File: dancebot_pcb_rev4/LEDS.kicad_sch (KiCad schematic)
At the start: 4 parts, among them J4 NeoPixel Left Eye, J9 NeoPixel Left Eye

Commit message: schematic ready for review!
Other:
- note added: "Hierarchical Labels"
- moved on the sheet: LED1, R11

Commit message: implemented some changes
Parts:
- added LED2: APT2012PGW, SamacSys_Parts:APT2012PGW, symbol Device:LED
- added R8: 1k, SamacSys_Parts:RESC2012X60N, symbol Device:R
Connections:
- net GND: now also R8.2
- new net: LED2.1 (K), R8.1
- new net IO45: LED2.2 (A)
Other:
- note added: "Heartbeat LED"

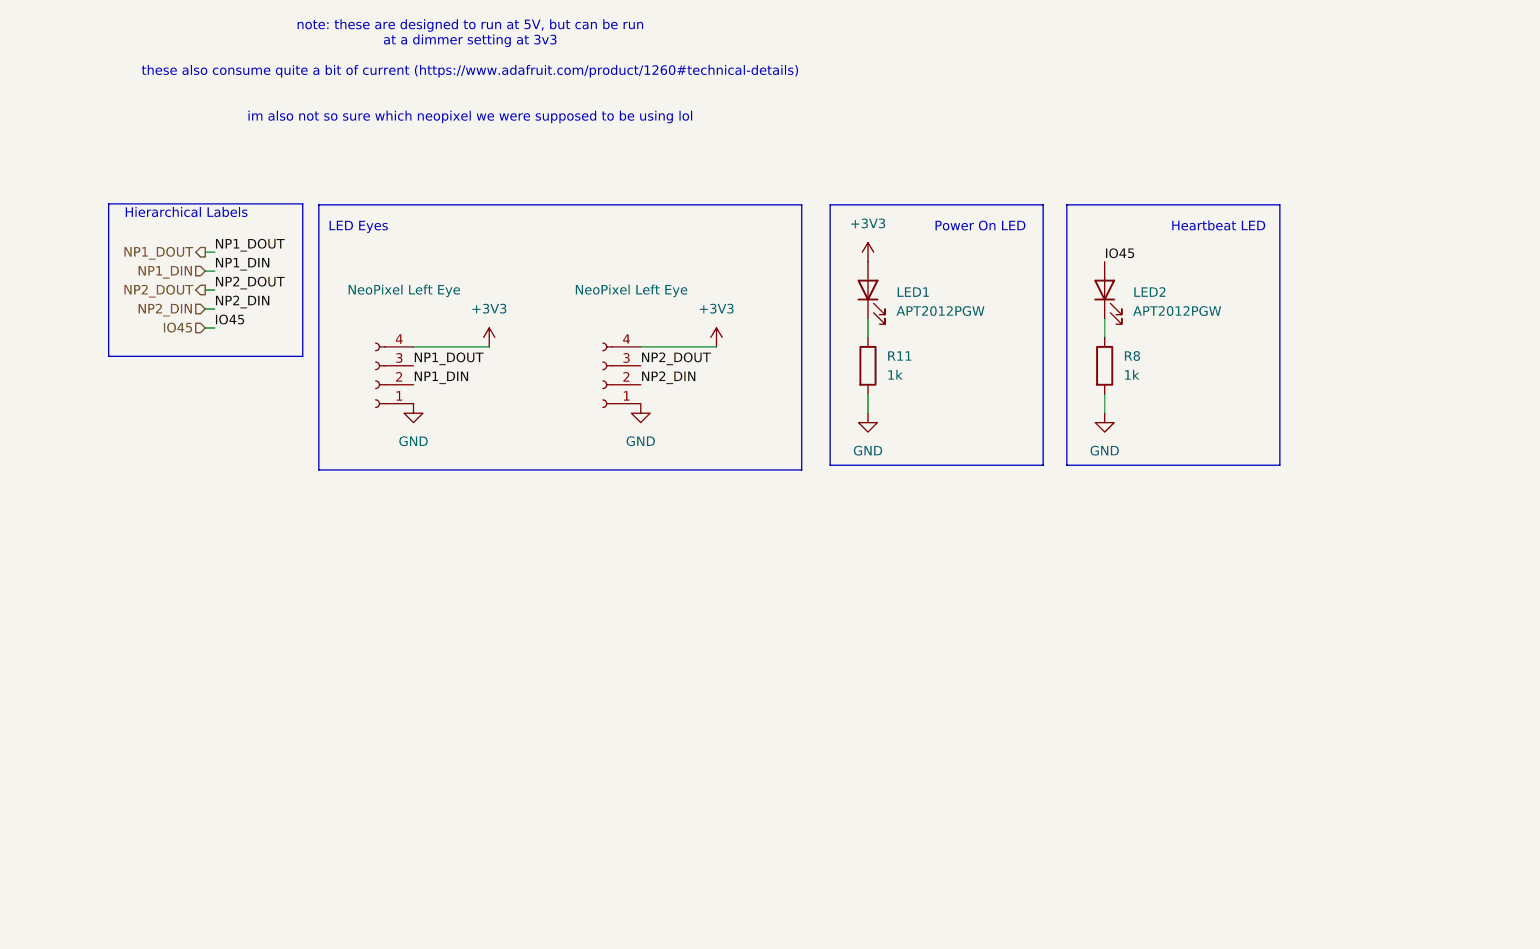
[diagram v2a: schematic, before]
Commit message: added more power leds. need to finish routing. fixed 3d models
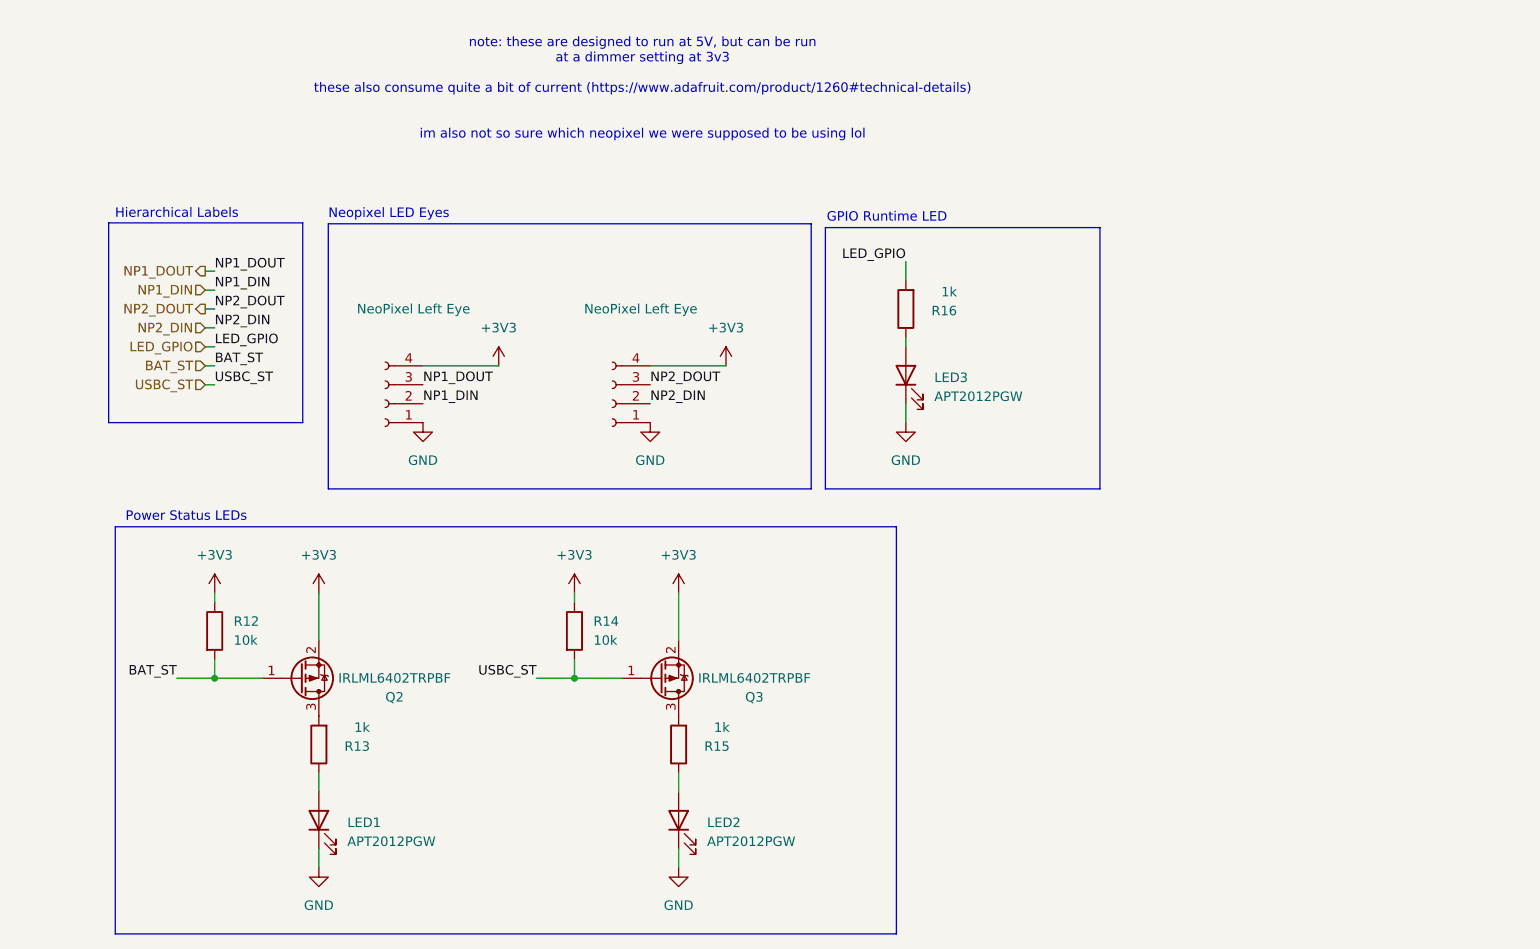
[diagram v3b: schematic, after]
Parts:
- removed R11, R8: 1k, SamacSys_Parts:RESC2012X60N, symbol Device:R
- added LED3: APT2012PGW, SamacSys_Parts:APT2012PGW, symbol Device:LED
- added Q2, Q3: IRLML6402TRPBF, Package_TO_SOT_SMD:SOT-23, symbol Transistor_FET:IRLML6402
- added R12, R14: 10k, SamacSys_Parts:RESC2012X60N, symbol Device:R
- added R13, R15, R16: 1k, SamacSys_Parts:RESC2012X60N, symbol Device:R
- renumbered J4 to J10
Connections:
- net +3V3: now also Q2.2 (S), Q3.2 (S), R12.1, R14.1; no longer LED1.2 (A)
- net GND: now also LED1.1 (K), LED2.1 (K), LED3.1 (K)
- net IO45: no longer names the net of LED2.2 (A)
- net IO45: now also R15.1
- new net: Q3.3 (D), R15.2
- new net: Q2.3 (D), R13.2
- new net: LED1.2 (A), R13.1
- new net: LED3.2 (A), R16.1
- new net BAT_ST: Q2.1 (G), R12.2
- new net LED_GPIO: R16.2
- new net USBC_ST: Q3.1 (G), R14.2
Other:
- note added: "GPIO Runtime LED"
- note added: "Neopixel LED Eyes"
- note added: "Power Status LEDs"
- note removed: "Heartbeat LED"
- note removed: "LED Eyes"
- note removed: "Power On LED"

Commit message: finished first layout. need to add polygon pours
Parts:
- J10: value NeoPixel Left Eye -> NeoPixel Right Eye
- renumbered Q2 to Q3, Q3 to Q4
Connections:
- net +3V3: now also J10.2 (Pin_2), J9.2 (Pin_2); no longer J10.4 (Pin_4), J9.4 (Pin_4)
- net NP1_DIN: now also J9.4 (Pin_4); no longer J9.2 (Pin_2)
- net NP2_DIN: now also J10.4 (Pin_4); no longer J10.2 (Pin_2)
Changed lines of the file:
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@@
 	(wire
 		(pts
-			(xy 86.36 36.83) (xy 96.52 36.83)
+			(xy 120.65 33.02) (xy 120.65 34.29)
 		)
 		(stroke
@@
 	(wire
 		(pts
-			(xy 120.65 33.02) (xy 120.65 34.29)
+			(xy 90.17 93.98) (xy 90.17 91.44)
 		)
 		(stroke
@@
 	(wire
 		(pts
-			(xy 90.17 93.98) (xy 90.17 91.44)
+			(xy 90.17 67.31) (xy 90.17 73.66)
 		)
 		(stroke
@@
 	(wire
 		(pts
-			(xy 90.17 67.31) (xy 90.17 73.66)
+			(xy 41.91 91.44) (xy 41.91 93.98)
 		)
 		(stroke
@@
 	(wire
 		(pts
-			(xy 41.91 91.44) (xy 41.91 93.98)
+			(xy 27.94 67.31) (xy 27.94 68.58)
 		)
 		(stroke
@@
 	(wire
 		(pts
-			(xy 27.94 67.31) (xy 27.94 68.58)
+			(xy 76.2 67.31) (xy 76.2 68.58)
 		)
 		(stroke
@@
 	(wire
 		(pts
-			(xy 76.2 67.31) (xy 76.2 68.58)
+			(xy 76.2 76.2) (xy 76.2 78.74)
 		)
 		(stroke
@@
 	(wire
 		(pts
-			(xy 76.2 76.2) (xy 76.2 78.74)
+			(xy 86.36 41.91) (xy 96.52 41.91)
 		)
 		(stroke
@@
 	(wire
 		(pts
-			(xy 55.88 36.83) (xy 66.04 36.83)
+			(xy 26.67 36.83) (xy 27.94 36.83)
 		)
 		(stroke
@@
 	(wire
 		(pts
-			(xy 26.67 36.83) (xy 27.94 36.83)
+			(xy 26.67 39.37) (xy 27.94 39.37)
 		)
 		(stroke
@@
 	(wire
 		(pts
-			(xy 26.67 39.37) (xy 27.94 39.37)
+			(xy 27.94 78.74) (xy 34.29 78.74)
 		)
 		(stroke
@@
 	(wire
 		(pts
-			(xy 27.94 78.74) (xy 34.29 78.74)
+			(xy 27.94 26.67) (xy 26.67 26.67)
 		)
 		(stroke
@@
 	(wire
 		(pts
-			(xy 27.94 26.67) (xy 26.67 26.67)
+			(xy 41.91 67.31) (xy 41.91 73.66)
 		)
 		(stroke
@@
 	(wire
 		(pts
-			(xy 41.91 67.31) (xy 41.91 73.66)
+			(xy 76.2 78.74) (xy 82.55 78.74)
 		)
 		(stroke
@@
 	(wire
 		(pts
-			(xy 76.2 78.74) (xy 82.55 78.74)
+			(xy 67.31 41.91) (xy 55.88 41.91)
 		)
 		(stroke
@@
 	)
 	(label "NP2_DIN"
-		(at 86.36 41.91 0)
+		(at 86.36 36.83 0)
 		(effects
 			(font
@@
 	)
 	(label "NP1_DIN"
-		(at 55.88 41.91 0)
+		(at 55.88 36.83 0)
 		(effects
 			(font
@@
 			)
 		)
-		(property "Value" "NeoPixel Left Eye"
-			(at 85.09 29.21 0)
+		(property "Value" "NeoPixel Right Eye"
+			(at 87.884 32.258 0)
 			(effects
 				(font
@@
 		(on_board yes)
 		(dnp no)
-		(property "Reference" "Q3"
+		(property "Reference" "Q4"
 			(at 100.33 81.28 0)
 			(effects
@@
 			(project "Dancebot_PCB"
 				(path "/21324b60-e5e7-4de6-a38d-f4cdf81a1b2c/d46550a5-946a-497c-941e-91cb76bf7d90"
-					(reference "Q3")
+					(reference "Q4")
 					(unit 1)
 				)
@@
 		)
 		(property "Value" "NeoPixel Left Eye"
-			(at 54.61 29.21 0)
+			(at 57.15 32.766 0)
 			(effects
 				(font
@@
 		(dnp no)
 		(fields_autoplaced yes)
-		(property "Reference" "#PWR050"
+		(property "Reference" "#PWR054"
 			(at 55.88 50.8 0)
 			(effects
@@
 			(project ""
 				(path "/21324b60-e5e7-4de6-a38d-f4cdf81a1b2c/d46550a5-946a-497c-941e-91cb76bf7d90"
-					(reference "#PWR050")
+					(reference "#PWR054")
 					(unit 1)
 				)
@@
 		(dnp no)
 		(fields_autoplaced yes)
-		(property "Reference" "#PWR057"
+		(property "Reference" "#PWR061"
 			(at 120.65 50.8 0)
 			(effects
@@
 			(project "Dancebot_PCB"
 				(path "/21324b60-e5e7-4de6-a38d-f4cdf81a1b2c/d46550a5-946a-497c-941e-91cb76bf7d90"
-					(reference "#PWR057")
+					(reference "#PWR061")
 					(unit 1)
 				)
@@
 	(symbol
 		(lib_id "power:+3V3")
-		(at 66.04 36.83 0)
+		(at 67.31 41.91 0)
 		(unit 1)
 		(exclude_from_sim no)
@@
 		(on_board yes)
 		(dnp no)
-		(fields_autoplaced yes)
-		(property "Reference" "#PWR051"
-			(at 66.04 40.64 0)
+		(property "Reference" "#PWR055"
+			(at 67.31 45.72 0)
 			(effects
 				(font
@@
 		)
 		(property "Value" "+3V3"
-			(at 66.04 31.75 0)
+			(at 69.342 38.1 0)
 			(effects
 				(font
@@
 		)
 		(property "Footprint" ""
-			(at 66.04 36.83 0)
+			(at 67.31 41.91 0)
 			(effects
 				(font
@@
 		)
 		(property "Datasheet" ""
-			(at 66.04 36.83 0)
+			(at 67.31 41.91 0)
 			(effects
 				(font
@@
 		)
 		(property "Description" "Power symbol creates a global label with name \"+3V3\""
-			(at 66.04 36.83 0)
+			(at 67.31 41.91 0)
 			(effects
 				(font
@@
 			(project ""
 				(path "/21324b60-e5e7-4de6-a38d-f4cdf81a1b2c/d46550a5-946a-497c-941e-91cb76bf7d90"
-					(reference "#PWR051")
+					(reference "#PWR055")
 					(unit 1)
 				)
@@
 		(on_board yes)
 		(dnp no)
-		(property "Reference" "Q2"
+		(property "Reference" "Q3"
 			(at 52.07 81.28 0)
 			(effects
@@
 			(project "Dancebot_PCB"
 				(path "/21324b60-e5e7-4de6-a38d-f4cdf81a1b2c/d46550a5-946a-497c-941e-91cb76bf7d90"
-					(reference "Q2")
+					(reference "Q3")
 					(unit 1)
 				)
@@
 	(symbol
 		(lib_id "power:+3V3")
-		(at 96.52 36.83 0)
+		(at 96.52 41.91 0)
 		(unit 1)
 		(exclude_from_sim no)
@@
 		(on_board yes)
 		(dnp no)
-		(fields_autoplaced yes)
-		(property "Reference" "#PWR056"
-			(at 96.52 40.64 0)
+		(property "Reference" "#PWR060"
+			(at 96.52 45.72 0)
 			(effects
 				(font
@@
 		)
 		(property "Value" "+3V3"
-			(at 96.52 31.75 0)
+			(at 100.33 39.37 0)
 			(effects
 				(font
@@
 		)
 		(property "Footprint" ""
-			(at 96.52 36.83 0)
+			(at 96.52 41.91 0)
 			(effects
 				(font
@@
 		)
 		(property "Datasheet" ""
-			(at 96.52 36.83 0)
+			(at 96.52 41.91 0)
 			(effects
 				(font
@@
 		)
 		(property "Description" "Power symbol creates a global label with name \"+3V3\""
-			(at 96.52 36.83 0)
+			(at 96.52 41.91 0)
 			(effects
 				(font
@@
 			(project "Dancebot_PCB"
 				(path "/21324b60-e5e7-4de6-a38d-f4cdf81a1b2c/d46550a5-946a-497c-941e-91cb76bf7d90"
-					(reference "#PWR056")
+					(reference "#PWR060")
 					(unit 1)
 				)
@@
 		(dnp no)
 		(fields_autoplaced yes)
-		(property "Reference" "#PWR049"
+		(property "Reference" "#PWR053"
 			(at 41.91 110.49 0)
 			(effects
@@
 			(project "Dancebot_PCB"
 				(path "/21324b60-e5e7-4de6-a38d-f4cdf81a1b2c/d46550a5-946a-497c-941e-91cb76bf7d90"
-					(reference "#PWR049")
+					(reference "#PWR053")
 					(unit 1)
 				)
@@
 		(dnp no)
 		(fields_autoplaced yes)
-		(property "Reference" "#PWR047"
+		(property "Reference" "#PWR051"
 			(at 27.94 71.12 0)
 			(effects
@@
 			(project "Dancebot_PCB"
 				(path "/21324b60-e5e7-4de6-a38d-f4cdf81a1b2c/d46550a5-946a-497c-941e-91cb76bf7d90"
-					(reference "#PWR047")
+					(reference "#PWR051")
 					(unit 1)
 				)
@@
 		(dnp no)
 		(fields_autoplaced yes)
-		(property "Reference" "#PWR055"
+		(property "Reference" "#PWR059"
 			(at 90.17 110.49 0)
 			(effects
@@
 			(project "Dancebot_PCB"
 				(path "/21324b60-e5e7-4de6-a38d-f4cdf81a1b2c/d46550a5-946a-497c-941e-91cb76bf7d90"
-					(reference "#PWR055")
+					(reference "#PWR059")
 					(unit 1)
 				)
@@
 		(dnp no)
 		(fields_autoplaced yes)
-		(property "Reference" "#PWR048"
+		(property "Reference" "#PWR052"
 			(at 41.91 71.12 0)
 			(effects
@@
 			(project "Dancebot_PCB"
 				(path "/21324b60-e5e7-4de6-a38d-f4cdf81a1b2c/d46550a5-946a-497c-941e-91cb76bf7d90"
-					(reference "#PWR048")
+					(reference "#PWR052")
 					(unit 1)
 				)
@@
 		(dnp no)
 		(fields_autoplaced yes)
-		(property "Reference" "#PWR054"
+		(property "Reference" "#PWR058"
 			(at 90.17 71.12 0)
 			(effects
@@
 			(project "Dancebot_PCB"
 				(path "/21324b60-e5e7-4de6-a38d-f4cdf81a1b2c/d46550a5-946a-497c-941e-91cb76bf7d90"
-					(reference "#PWR054")
+					(reference "#PWR058")
 					(unit 1)
 				)
@@
 		(dnp no)
 		(fields_autoplaced yes)
-		(property "Reference" "#PWR052"
+		(property "Reference" "#PWR056"
 			(at 76.2 71.12 0)
 			(effects
@@
 			(project "Dancebot_PCB"
 				(path "/21324b60-e5e7-4de6-a38d-f4cdf81a1b2c/d46550a5-946a-497c-941e-91cb76bf7d90"
-					(reference "#PWR052")
+					(reference "#PWR056")
 					(unit 1)
 				)
@@
 		(dnp no)
 		(fields_autoplaced yes)
-		(property "Reference" "#PWR053"
+		(property "Reference" "#PWR057"
 			(at 86.36 50.8 0)
 			(effects
@@
 			(project "Dancebot_PCB"
 				(path "/21324b60-e5e7-4de6-a38d-f4cdf81a1b2c/d46550a5-946a-497c-941e-91cb76bf7d90"
-					(reference "#PWR053")
+					(reference "#PWR057")
 					(unit 1)
 				)

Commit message: search replaced mouser.co.uk with mouser.com
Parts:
- LED1, LED2, LED3: Mouser Price/Stock https://www.mouser.co.uk/ProductDetail/Kingbright/APT2012PG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 -> https://www.mouser.com/ProductDetail/Kingbright/APT2012PGW?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
- Q3, Q4: Mouser Price/Stock https://www.mouser.co.uk/ProductDetail/Infineon-Technologie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 -> https://www.mouser.com/ProductDetail/Infineon-Technologies/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
- R12, R14: Mouser Price/Stock https://www.mouser.co.uk/ProductDetail/Welwyn-Components-TT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 -> https://www.mouser.com/ProductDetail/Welwyn-Components-TT-E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
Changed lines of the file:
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@@
 			)
 		)
-		(property "Mouser Price/Stock" "https://www.mouser.co.uk/ProductDetail/Infineon-Technologies/IRLML6402TRPBF?qs=9%252BKlkBgLFf0HuZuONx2Ewg%3D%3D"
+		(property "Mouser Price/Stock" "https://www.mouser.com/ProductDetail/Infineon-Technologies/IRLML6402TRPBF?qs=9%252BKlkBgLFf0HuZuONx2Ewg%3D%3D"
 			(at 87.63 78.74 0)
 			(effects
@@
 			)
 		)
-		(property "Mouser Price/Stock" "https://www.mouser.co.uk/ProductDetail/Welwyn-Components-TT-Electronics/ASC0805-10KFT5?qs=69TQa8YF5Y7dvxAm%2FqWqSQ%3D%3D"
+		(property "Mouser Price/Stock" "https://www.mouser.com/ProductDetail/Welwyn-Components-TT-Electronics/ASC0805-10KFT5?qs=69TQa8YF5Y7dvxAm%2FqWqSQ%3D%3D"
 			(at 41.91 668.58 0)
 			(effects
@@
 			)
 		)
-		(property "Mouser Price/Stock" "https://www.mouser.co.uk/ProductDetail/Infineon-Technologies/IRLML6402TRPBF?qs=9%252BKlkBgLFf0HuZuONx2Ewg%3D%3D"
+		(property "Mouser Price/Stock" "https://www.mouser.com/ProductDetail/Infineon-Technologies/IRLML6402TRPBF?qs=9%252BKlkBgLFf0HuZuONx2Ewg%3D%3D"
 			(at 39.37 78.74 0)
 			(effects
@@
 			)
 		)
-		(property "Mouser Price/Stock" "https://www.mouser.co.uk/ProductDetail/Kingbright/APT2012PGW?qs=SxaZfIVsCL2edu2fuRiRPw%3D%3D"
+		(property "Mouser Price/Stock" "https://www.mouser.com/ProductDetail/Kingbright/APT2012PGW?qs=SxaZfIVsCL2edu2fuRiRPw%3D%3D"
 			(at 683.82 85.09 0)
 			(effects
@@
 			)
 		)
-		(property "Mouser Price/Stock" "https://www.mouser.co.uk/ProductDetail/Kingbright/APT2012PGW?qs=SxaZfIVsCL2edu2fuRiRPw%3D%3D"
+		(property "Mouser Price/Stock" "https://www.mouser.com/ProductDetail/Kingbright/APT2012PGW?qs=SxaZfIVsCL2edu2fuRiRPw%3D%3D"
 			(at 635.56 85.09 0)
 			(effects
@@
 			)
 		)
-		(property "Mouser Price/Stock" "https://www.mouser.co.uk/ProductDetail/Kingbright/APT2012PGW?qs=SxaZfIVsCL2edu2fuRiRPw%3D%3D"
+		(property "Mouser Price/Stock" "https://www.mouser.com/ProductDetail/Kingbright/APT2012PGW?qs=SxaZfIVsCL2edu2fuRiRPw%3D%3D"
 			(at 714.3 25.4 0)
 			(effects
@@
 			)
 		)
-		(property "Mouser Price/Stock" "https://www.mouser.co.uk/ProductDetail/Welwyn-Components-TT-Electronics/ASC0805-10KFT5?qs=69TQa8YF5Y7dvxAm%2FqWqSQ%3D%3D"
+		(property "Mouser Price/Stock" "https://www.mouser.com/ProductDetail/Welwyn-Components-TT-Electronics/ASC0805-10KFT5?qs=69TQa8YF5Y7dvxAm%2FqWqSQ%3D%3D"
 			(at 90.17 668.58 0)
 			(effects
